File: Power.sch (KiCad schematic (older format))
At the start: 10 parts

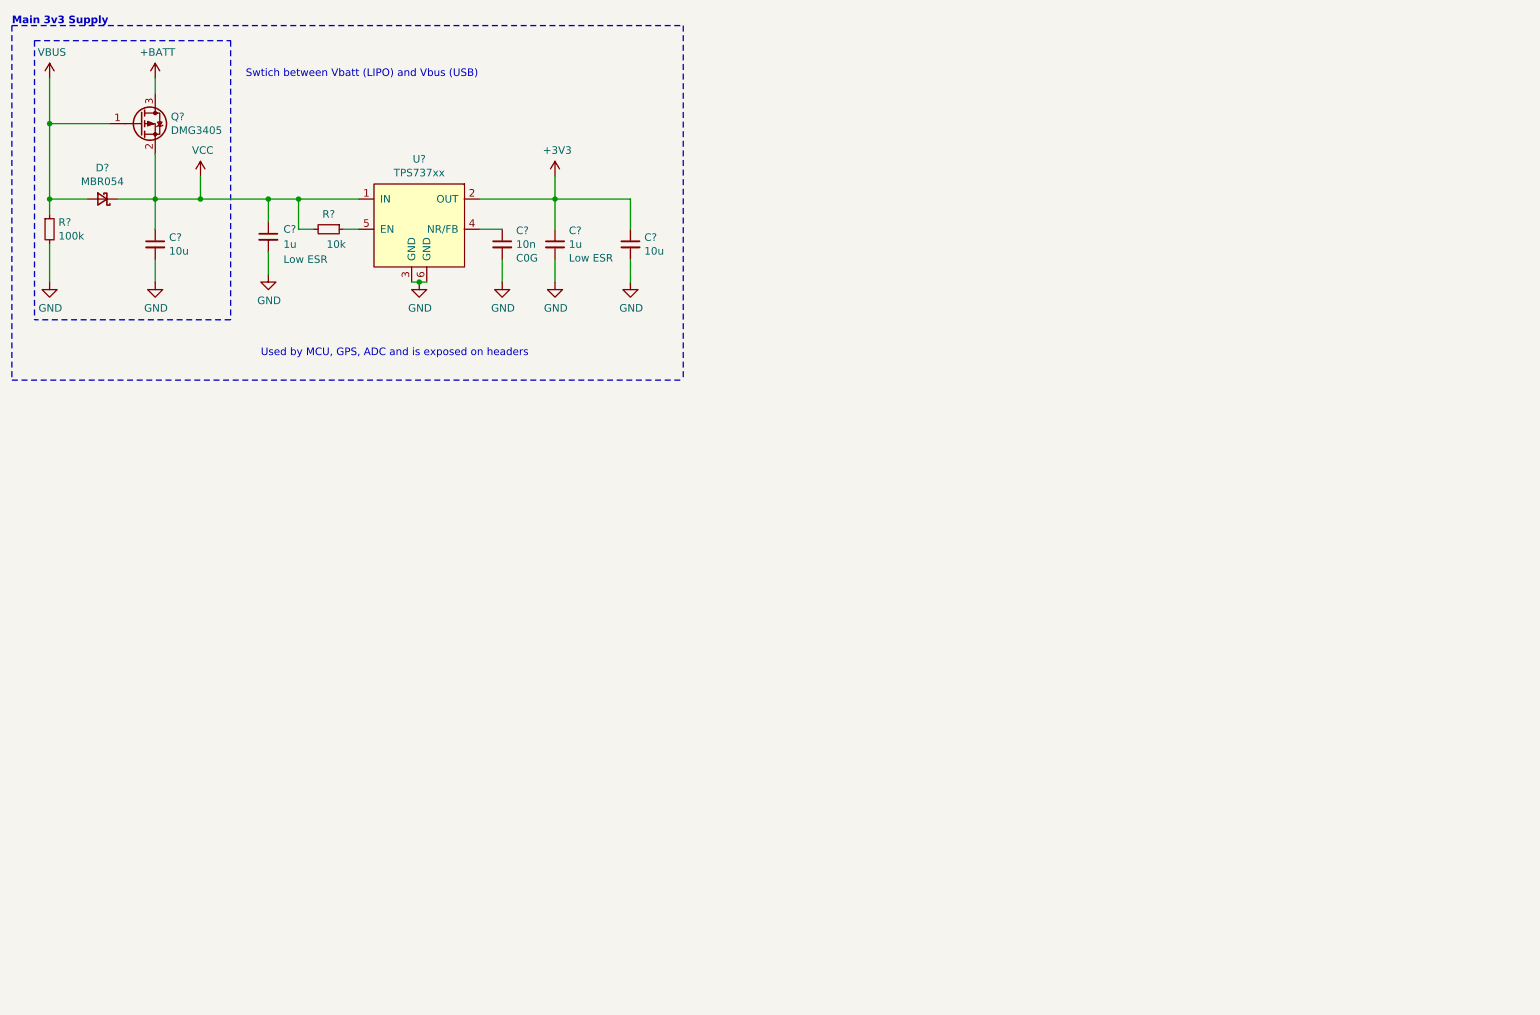
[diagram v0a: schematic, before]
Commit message: Design Power (Dual Rail) section
Also add USB-C connection
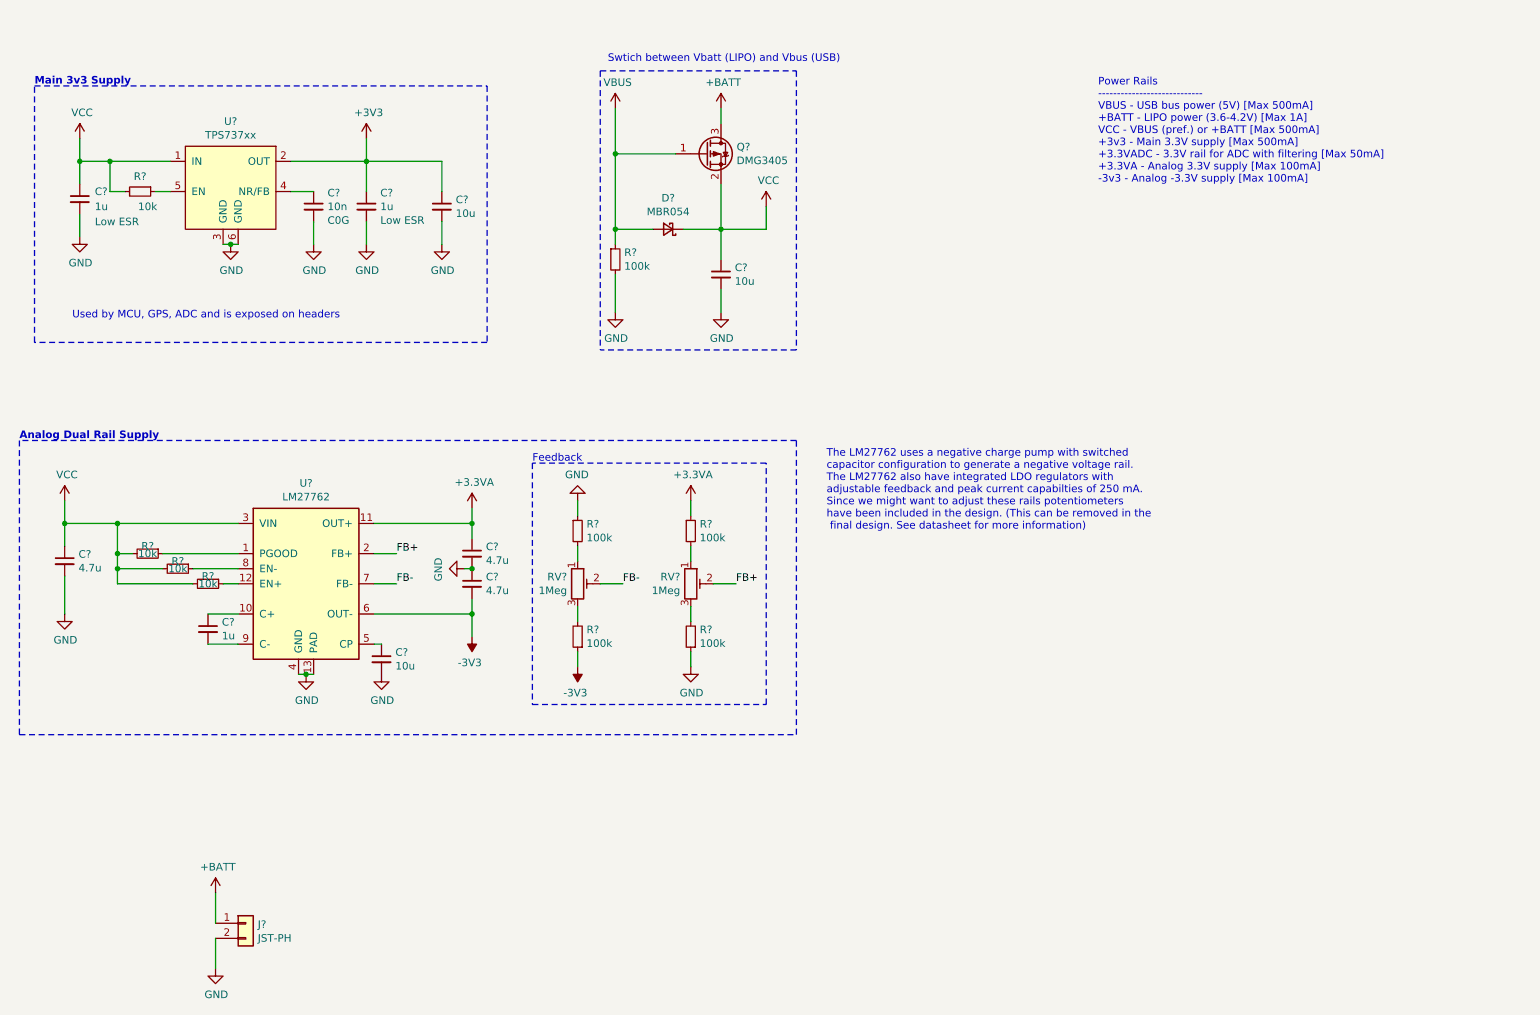
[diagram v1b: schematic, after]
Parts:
- added C? (x3): 4.7u, symbol Device:C_Small
- added C?: 1u, symbol Device:C_Small
- added C?: 10u, symbol Device:C_Small
- added J?: JST-PH, symbol Connector_Generic:Conn_01x02
- added R? (x4): 100k, symbol Device:R_Small
- added R? (x3): 10k, symbol Device:R_Small
- added RV? (x2): 1Meg, symbol Device:R_POT_TRIM
- added U?: LM27762, Package_SON:WSON-12-1EP_3x2mm_P0.5mm_EP1x2.65_ThermalVias, symbol Regulator_SwitchedCapacitor:LM27762
- D?: MPN (none) -> MBR054
- Q?: MPN (none) -> DMG3405
- U?: MPN (none) -> TPS73733DCQR; Mfr. (none) -> Texas Instruments
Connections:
- net +BATT: now also J?.1 (Pin_1)
- net GND: now also C?.1, C?.2, C?.2, C?.2, J?.2 (Pin_2), R?.1, R?.1, U?.13 (PAD), U?.4 (GND)
- net VCC: now also C?.1, R?.2, R?.2, R?.2, U?.3 (VIN)
- new net: R?.2, RV?.1 (x2)
- new net: R?.2, RV?.3 (x2)
- new net: R?.1, U?.1 (PGOOD)
- new net: C?.1, U?.10 (C+)
- new net: R?.1, U?.12 (EN+)
- new net: C?.1, U?.5 (CP)
- new net: R?.1, U?.8 (EN-)
- new net: C?.2, U?.9 (C-)
- new net +3.3VA: C?.1, R?.1, U?.11 (OUT+)
- new net -3V3: C?.2, R?.1, U?.6 (OUT-)
- new net FB+: RV?.2, U?.2 (FB+)
- new net FB-: RV?.2, U?.7 (FB-)
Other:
- note added: "Analog Dual Rail Supply"
- note added: "Feedback"
- note added: "Power Rails\n----------------------------\nVBUS - USB bus power (5V) [Max 500mA]\n+BATT - LIPO power (3.6-4.2V) [Max 1A]\nVCC - VBUS (pref.) or +BATT [Max 500mA]\n+3v3 - Main 3.3V supply [Max 500mA]\n+3.3VADC - 3.3V rail for ADC with filtering [Max 50mA]\n+3.3VA - Analog 3.3V supply [Max 100mA]\n-3v3 - Analog -3.3V supply [Max 100mA]"
- note added: "The LM27762 uses a negative charge pump with switched \ncapacitor configuration to generate a negative voltage rail. \nThe LM27762 also have integrated LDO regulators with \nadjustable feedback and peak current capabilties of 250 mA. \nSince we might want to adjust these rails potentiometers \nhave been included in the design. (This can be removed in the\n final design. See datasheet for more inf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"
- moved on the sheet: C?, D?, Q?, R?, U?

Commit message: Design LIPO charge circuit
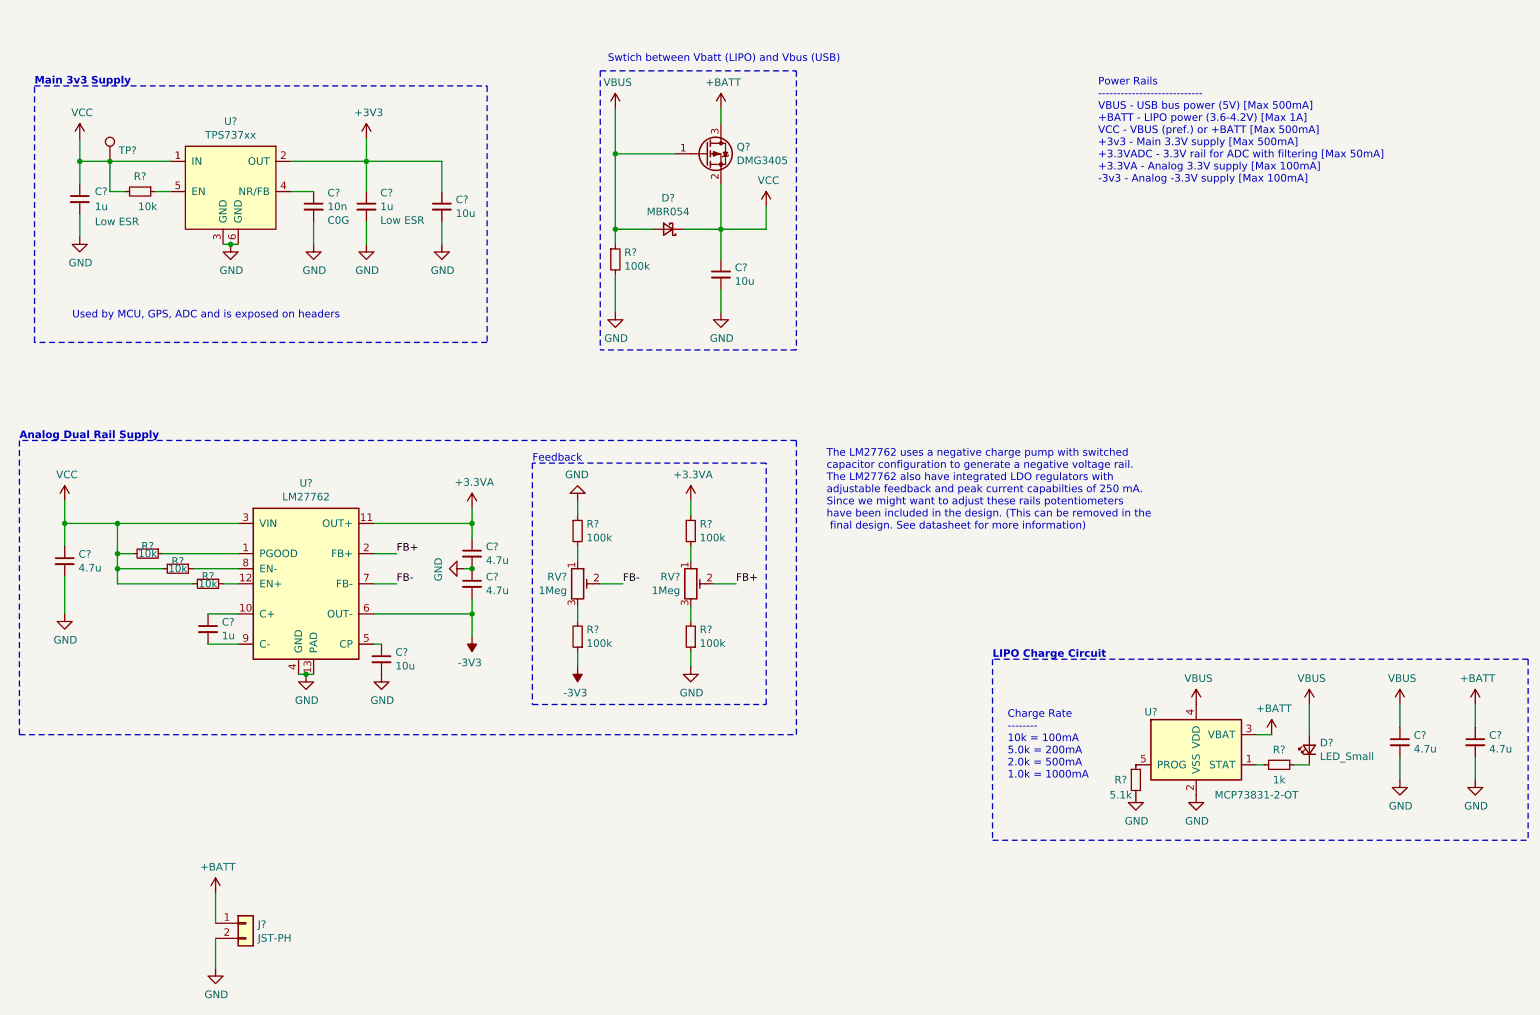
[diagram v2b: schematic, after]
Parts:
- added C? (x2): 4.7u, symbol Device:C_Small
- added D?: LED_Small, symbol Device:LED_Small
- added R?: 1k, symbol Device:R_Small
- added R?: 5.1k, symbol Device:R_Small
- added TP?: TestPoint, symbol Connector:TestPoint
- added U?: MCP73831-2-OT, Package_TO_SOT_SMD:SOT-23-5, symbol Battery_Management:MCP73831-2-OT
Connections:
- net +BATT: now also C?.1, U?.3 (VBAT)
- net GND: now also C?.2, C?.2, R?.2, U?.2 (VSS)
- net VBUS: now also C?.1, D?.2 (A), U?.4 (VDD)
- net VCC: now also TP?.1
- new net: R?.2, U?.1 (STAT)
- new net: R?.1, U?.5 (PROG)
- new net: D?.1 (K), R?.1
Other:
- note added: "Charge Rate\n--------\n10k = 100mA\n5.0k = 200mA\n2.0k = 500mA\n1.0k = 1000mA"
- note added: "LIPO Charge Circuit"
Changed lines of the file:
@@
 Wire Wire Line
 	2100 6750 2100 6550
+$Comp
+L Connector:TestPoint TP?
+U 1 1 5EEECC26
+P 1400 1700
+F 0 "TP?" H 1458 1772 50  0000 L CNN
+F 1 "TestPoint" H 1458 1727 50  0001 L CNN
+F 2 "" H 1600 1700 50  0001 C CNN
+F 3 "~" H 1600 1700 50  0001 C CNN
+	1    1400 1700
+	1    0    0    -1
+$EndComp
+$Comp
+L Battery_Management:MCP73831-2-OT U?
+U 1 1 5EEF3F74
+P 8600 5600
+F 0 "U?" H 8300 5850 50  0000 C CNN
+F 1 "MCP73831-2-OT" H 9000 5300 50  0000 C CNN
+F 2 "Package_TO_SOT_SMD:SOT-23-5" H 8650 5350 50  0001 L CIN
+F 3 "http://ww1.microchip.com/downloads/en/DeviceDoc/20001984g.pdf" H 8450 5550 50  0001 C CNN
+F 4 "Microchip" H 8600 5600 50  0001 C CNN "Mfr."
+F 5 "MCP73831-2-OT" H 8600 5600 50  0001 C CNN "MPN"
+	1    8600 5600
+	1    0    0    -1
+$EndComp
+$Comp
+L power:VBUS #PWR?
+U 1 1 5EEF7DD5
+P 8600 5300
+F 0 "#PWR?" H 8600 5150 50  0001 C CNN
+F 1 "VBUS" H 8615 5473 50  0000 C CNN
+F 2 "" H 8600 5300 50  0001 C CNN
+F 3 "" H 8600 5300 50  0001 C CNN
+	1    8600 5300
+	1    0    0    -1
+$EndComp
+$Comp
+L power:VBUS #PWR?
+U 1 1 5EEFA16D
+P 9950 5300
+F 0 "#PWR?" H 9950 5150 50  0001 C CNN
+F 1 "VBUS" H 9965 5473 50  0000 C CNN
+F 2 "" H 9950 5300 50  0001 C CNN
+F 3 "" H 9950 5300 50  0001 C CNN
+	1    9950 5300
+	1    0    0    -1
+$EndComp
+$Comp
+L power:GND #PWR?
+U 1 1 5EEFA9F7
+P 8200 5900
+F 0 "#PWR?" H 8200 5650 50  0001 C CNN
+F 1 "GND" H 8205 5727 50  0000 C CNN
+F 2 "" H 8200 5900 50  0001 C CNN
+F 3 "" H 8200 5900 50  0001 C CNN
+	1    8200 5900
+	1    0    0    -1
+$EndComp
+$Comp
+L power:GND #PWR?
+U 1 1 5EEFB815
+P 9950 5800
+F 0 "#PWR?" H 9950 5550 50  0001 C CNN
+F 1 "GND" H 9955 5627 50  0000 C CNN
+F 2 "" H 9950 5800 50  0001 C CNN
+F 3 "" H 9950 5800 50  0001 C CNN
+	1    9950 5800
+	1    0    0    -1
+$EndComp
+Wire Wire Line
+	9950 5800 9950 5650
+Wire Wire Line
+	9950 5450 9950 5300
+$Comp
+L Device:C_Small C?
+U 1 1 5EF00B7E
+P 9950 5550
+F 0 "C?" H 10042 5596 50  0000 L CNN
+F 1 "4.7u" H 10042 5505 50  0000 L CNN
+F 2 "" H 9950 5550 50  0001 C CNN
+F 3 "~" H 9950 5550 50  0001 C CNN
+F 4 "Low ESR" H 9950 5550 50  0001 C CNN "Notes"
+F 5 "MuRata" H 9950 5550 50  0001 C CNN "Mfr."
+F 6 "GRM188R60J475KE19D" H 9950 5550 50  0001 C CNN "MPN"
+	1    9950 5550
+	1    0    0    -1
+$EndComp
+$Comp
+L power:GND #PWR?
+U 1 1 5EF0659B
+P 10450 5800
+F 0 "#PWR?" H 10450 5550 50  0001 C CNN
+F 1 "GND" H 10455 5627 50  0000 C CNN
+F 2 "" H 10450 5800 50  0001 C CNN
+F 3 "" H 10450 5800 50  0001 C CNN
+	1    10450 5800
+	1    0    0    -1
+$EndComp
+Wire Wire Line
+	10450 5800 10450 5650
+Wire Wire Line
+	10450 5450 10450 5300
+$Comp
+L Device:C_Small C?
+U 1 1 5EF065A6
+P 10450 5550
+F 0 "C?" H 10542 5596 50  0000 L CNN
+F 1 "4.7u" H 10542 5505 50  0000 L CNN
+F 2 "" H 10450 5550 50  0001 C CNN
+F 3 "~" H 10450 5550 50  0001 C CNN
+F 4 "Low ESR" H 10450 5550 50  0001 C CNN "Notes"
+F 5 "MuRata" H 10450 5550 50  0001 C CNN "Mfr."
+F 6 "GRM188R60J475KE19D" H 10450 5550 50  0001 C CNN "MPN"
+	1    10450 5550
+	1    0    0    -1
+$EndComp
+$Comp
+L power:+BATT #PWR?
+U 1 1 5EF082DD
+P 10450 5300
+F 0 "#PWR?" H 10450 5150 50  0001 C CNN
+F 1 "+BATT" H 10465 5473 50  0000 C CNN
+F 2 "" H 10450 5300 50  0001 C CNN
+F 3 "" H 10450 5300 50  0001 C CNN
+	1    10450 5300
+	1    0    0    -1
+$EndComp
+$Comp
+L power:+BATT #PWR?
+U 1 1 5EF0C060
+P 9100 5500
+F 0 "#PWR?" H 9100 5350 50  0001 C CNN
+F 1 "+BATT" H 9115 5673 50  0000 C CNN
+F 2 "" H 9100 5500 50  0001 C CNN
+F 3 "" H 9100 5500 50  0001 C CNN
+	1    9100 5500
+	1    0    0    -1
+$EndComp
+Wire Wire Line
+	9100 5500 9000 5500
+$Comp
+L Device:LED_Small D?
+U 1 1 5EF0E889
+P 9350 5600
+F 0 "D?" V 9396 5530 50  0000 R CNN
+F 1 "LED_Small" V 9305 5530 50  0000 R CNN
+F 2 "" V 9350 5600 50  0001 C CNN
+F 3 "~" V 9350 5600 50  0001 C CNN
+	1    9350 5600
+	0    -1   -1   0
+$EndComp
+$Comp
+L Device:R_Small R?
+U 1 1 5EF0F677
+P 9150 5700
+F 0 "R?" V 9050 5700 50  0000 C CNN
+F 1 "1k" V 9250 5700 50  0000 C CNN
+F 2 "" H 9150 5700 50  0001 C CNN
+F 3 "~" H 9150 5700 50  0001 C CNN
+	1    9150 5700
+	0    1    1    0
+$EndComp
+Wire Wire Line
+	9250 5700 9350 5700
+Wire Wire Line
+	9050 5700 9000 5700
+$Comp
+L power:VBUS #PWR?
+U 1 1 5EF13DD3
+P 9350 5300
+F 0 "#PWR?" H 9350 5150 50  0001 C CNN
+F 1 "VBUS" H 9365 5473 50  0000 C CNN
+F 2 "" H 9350 5300 50  0001 C CNN
+F 3 "" H 9350 5300 50  0001 C CNN
+	1    9350 5300
+	1    0    0    -1
+$EndComp
+Wire Wire Line
+	9350 5300 9350 5500
+$Comp
+L Device:R_Small R?
+U 1 1 5EF16CE7
+P 8200 5800
+F 0 "R?" H 8100 5800 50  0000 C CNN
+F 1 "5.1k" H 8100 5700 50  0000 C CNN
+F 2 "" H 8200 5800 50  0001 C CNN
+F 3 "~" H 8200 5800 50  0001 C CNN
+	1    8200 5800
+	1    0    0    -1
+$EndComp
+$Comp
+L power:GND #PWR?
+U 1 1 5EF19F9D
+P 8600 5900
+F 0 "#PWR?" H 8600 5650 50  0001 C CNN
+F 1 "GND" H 8605 5727 50  0000 C CNN
+F 2 "" H 8600 5900 50  0001 C CNN
+F 3 "" H 8600 5900 50  0001 C CNN
+	1    8600 5900
+	1    0    0    -1
+$EndComp
+Text Notes 7350 5800 0    50   ~ 0
+Charge Rate\n--------\n10k = 100mA\n5.0k = 200mA\n2.0k = 500mA\n1.0k = 1000mA
+Wire Notes Line
+	10800 5000 7250 5000
+Wire Notes Line
+	7250 5000 7250 6200
+Wire Notes Line
+	7250 6200 10800 6200
+Wire Notes Line
+	10800 5000 10800 6200
+Text Notes 7250 5000 0    50   ~ 10
+LIPO Charge Circuit
 $EndSCHEMATC

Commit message: Design Mic. Board
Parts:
- removed J?: JST-PH, symbol Connector_Generic:Conn_01x02
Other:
- note added: "Power Rails\n----------------------------\nVBUS - USB bus power (5V) [Max 500mA]\n+BATT - LIPO power (3.6-4.2V) [Max 1A]\nVCC - VBUS (pref.) or +BATT [Max 500mA]\nVDD - GPS backup battery\n+3v3 - Main 3.3V supply [Max 500mA]\n+3.3VADC - 3.3V rail for ADC with filtering [Max 50mA]\n+3.3VA - Analog 3.3V supply [Max 100mA]\n-3v3 - Analog -3.3V supply [Max 100mA]"
- note removed: "Power Rails\n----------------------------\nVBUS - USB bus power (5V) [Max 500mA]\n+BATT - LIPO power (3.6-4.2V) [Max 1A]\nVCC - VBUS (pref.) or +BATT [Max 500mA]\n+3v3 - Main 3.3V supply [Max 500mA]\n+3.3VADC - 3.3V rail for ADC with filtering [Max 50mA]\n+3.3VA - Analog 3.3V supply [Max 100mA]\n-3v3 - Analog -3.3V supply [Max 100mA]"
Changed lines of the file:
@@
 $Descr A4 11693 8268
 encoding utf-8
-Sheet 12 13
+Sheet 12 14
 Title ""
 Date ""
@@
 $EndComp
 Text Notes 7950 1850 0    50   ~ 0
-Power Rails\n----------------------------\nVBUS - USB bus power (5V) [Max 500mA]\n+BATT - LIPO power (3.6-4.2V) [Max 1A]\nVCC - VBUS (pref.) or +BATT [Max 500mA]\n+3v3 - Main 3.3V supply [Max 500mA]\n+3.3VADC - 3.3V rail for ADC with filtering [Max 50mA]\n+3.3VA - Analog 3.3V supply [Max 100mA]\n-3v3 - Analog -3.3V supply [Max 100mA]
+Power Rails\n----------------------------\nVBUS - USB bus power (5V) [Max 500mA]\n+BATT - LIPO power (3.6-4.2V) [Max 1A]\nVCC - VBUS (pref.) or +BATT [Max 500mA]\nVDD - GPS backup battery\n+3v3 - Main 3.3V supply [Max 500mA]\n+3.3VADC - 3.3V rail for ADC with filtering [Max 50mA]\n+3.3VA - Analog 3.3V supply [Max 100mA]\n-3v3 - Analog -3.3V supply [Max 100mA]
 $Comp
 L power:+3.3VA #PWR?
@@
 The LM27762 uses a negative charge pump with switched \ncapacitor configuration to generate a negative voltage rail. \nThe LM27762 also have integrated LDO regulators with \nadjustable feedback and peak current capabilties of 250 mA. \nSince we might want to adjust these rails potentiometers \nhave been included in the design. (This can be removed in the\n final design. See datasheet for more information)
 $Comp
-L Connector_Generic:Conn_01x02 J?
-U 1 1 5EEA4055
-P 2300 6750
-F 0 "J?" H 2380 6742 50  0000 L CNN
-F 1 "JST-PH" H 2380 6651 50  0000 L CNN
-F 2 "" H 2300 6750 50  0001 C CNN
-F 3 "~" H 2300 6750 50  0001 C CNN
-	1    2300 6750
-	1    0    0    -1
-$EndComp
-$Comp
-L power:+BATT #PWR?
-U 1 1 5EEABDA3
-P 2100 6550
-F 0 "#PWR?" H 2100 6400 50  0001 C CNN
-F 1 "+BATT" H 2115 6723 50  0000 C CNN
-F 2 "" H 2100 6550 50  0001 C CNN
-F 3 "" H 2100 6550 50  0001 C CNN
-	1    2100 6550
-	1    0    0    -1
-$EndComp
-$Comp
-L power:GND #PWR?
-U 1 1 5EEAE63F
-P 2100 7050
-F 0 "#PWR?" H 2100 6800 50  0001 C CNN
-F 1 "GND" H 2105 6877 50  0000 C CNN
-F 2 "" H 2100 7050 50  0001 C CNN
-F 3 "" H 2100 7050 50  0001 C CNN
-	1    2100 7050
-	1    0    0    -1
-$EndComp
-Wire Wire Line
-	2100 7050 2100 6850
-Wire Wire Line
-	2100 6750 2100 6550
-$Comp
 L Connector:TestPoint TP?
